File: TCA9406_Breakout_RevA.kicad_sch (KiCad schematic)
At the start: 23 parts, among them J1 Connector A, J2 Connector B, U1 TCA9406DC

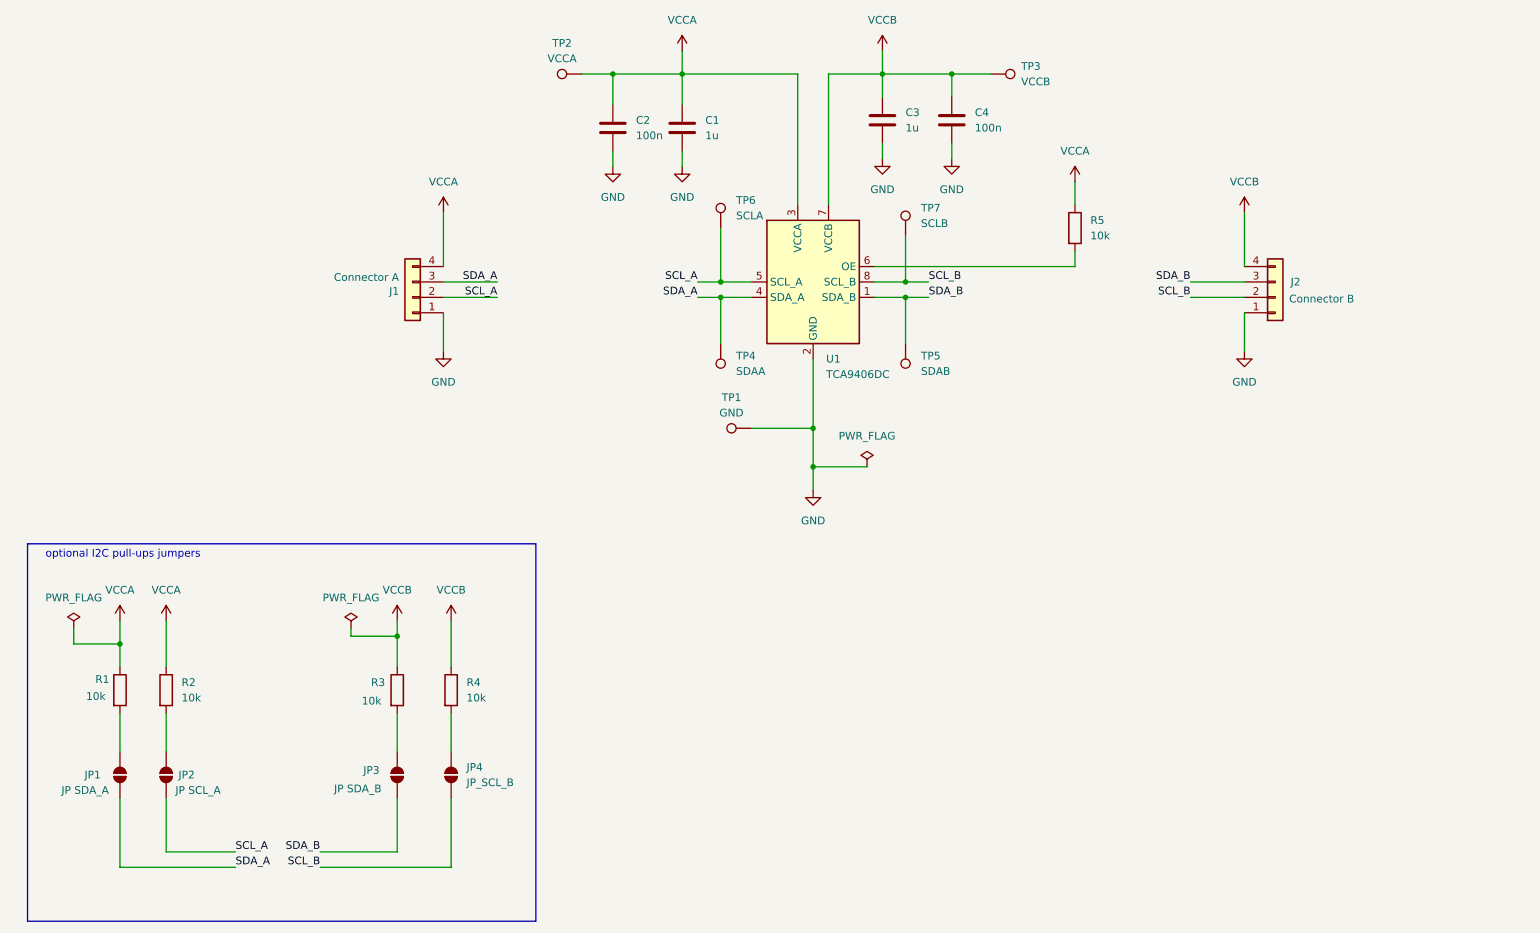
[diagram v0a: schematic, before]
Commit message: Add comprehensive README.md
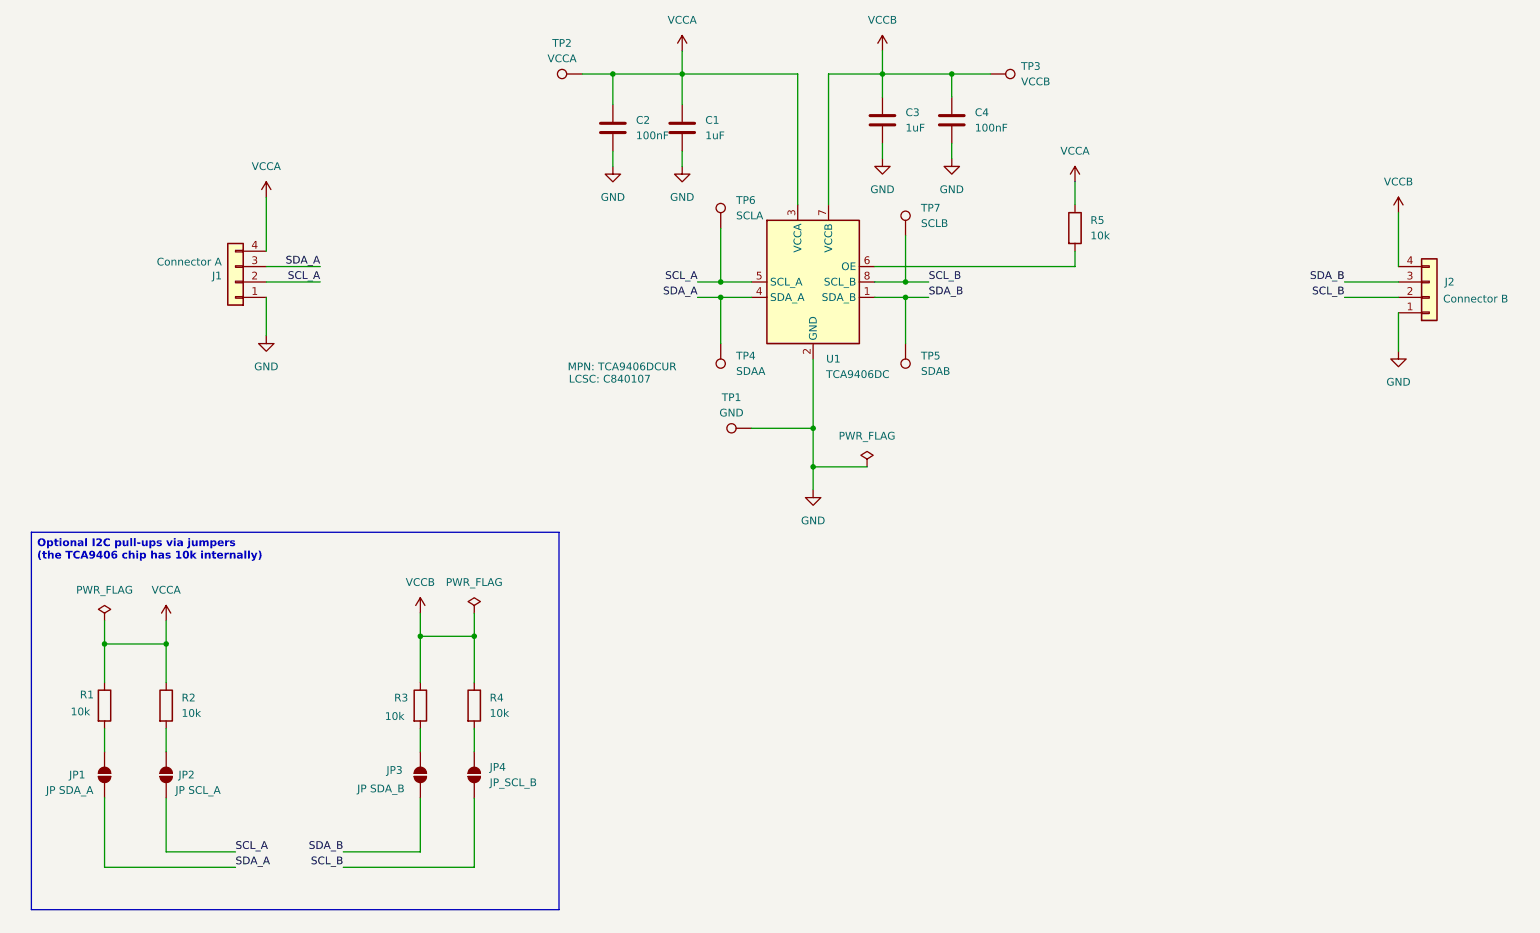
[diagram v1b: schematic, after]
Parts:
- C1, C3: value 1u -> 1uF
- C2, C4: value 100n -> 100nF
- TP1, TP2, TP3, TP4, TP5, TP6, TP7: now left out of the parts list
- U1: LCSC (none) -> C840107; MPN (none) -> TCA9406DCUR
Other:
- note removed: "optional I2C pull-ups jumpers"
- company: Ivory Electronics -> Ivory Electronics Ltd
- moved on the sheet: J1, J2, JP1, JP3, JP4, R1, R2, R3, R4
